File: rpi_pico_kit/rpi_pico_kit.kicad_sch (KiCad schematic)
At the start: 2 parts, among them U1 Pico, U2 RP2040

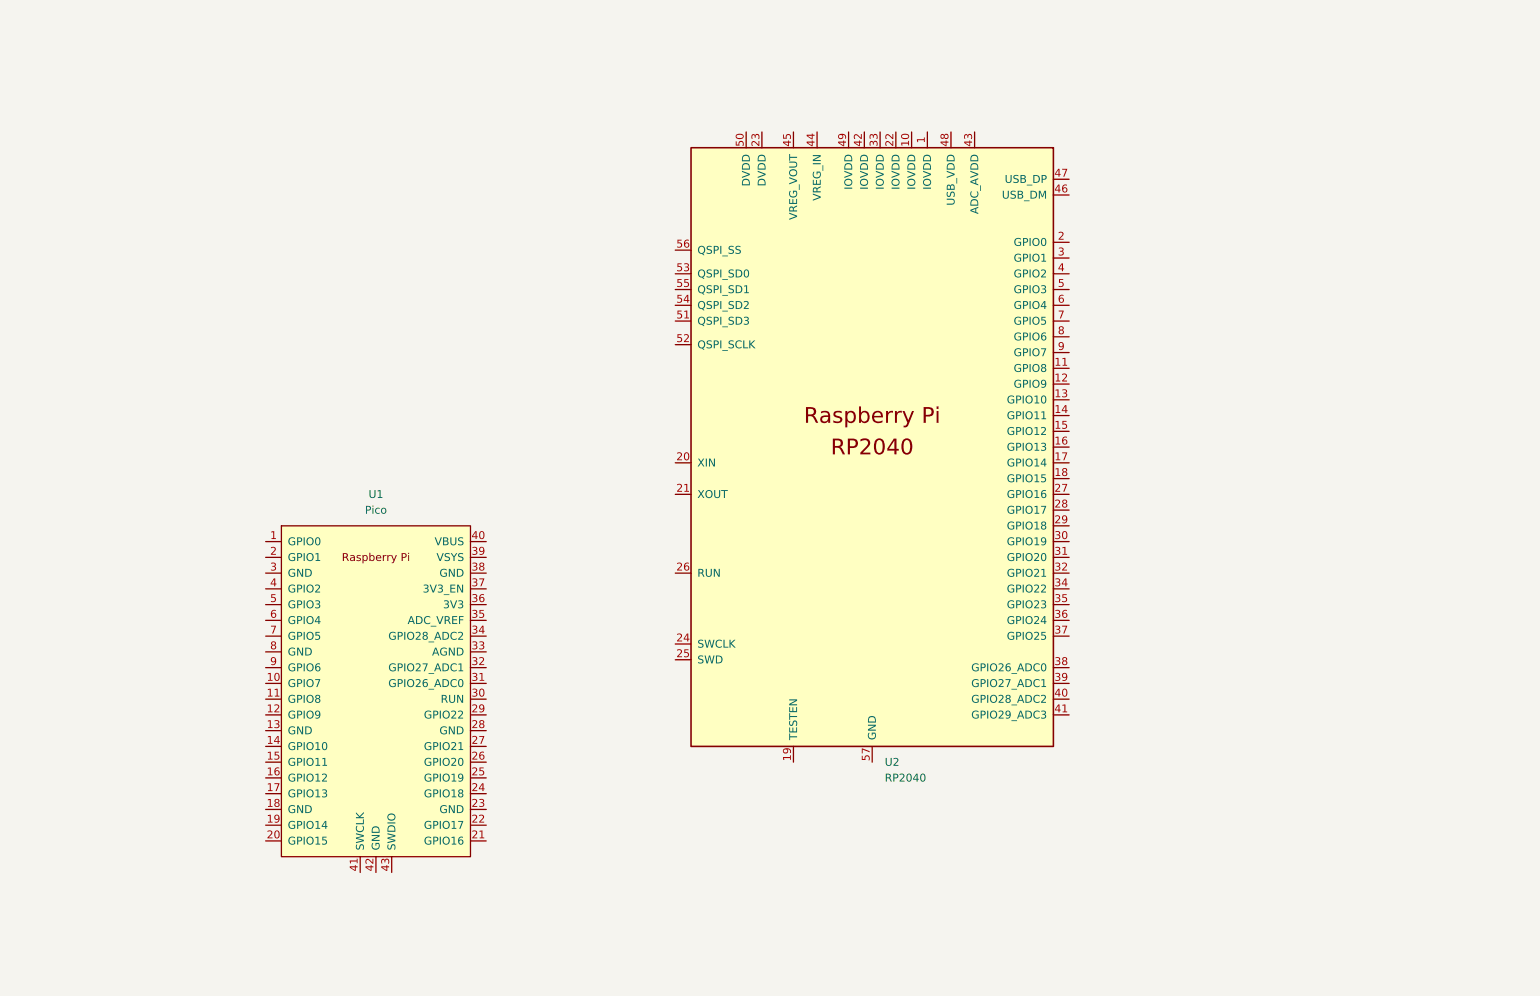
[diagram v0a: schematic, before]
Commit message: added second rpi pico as debugger
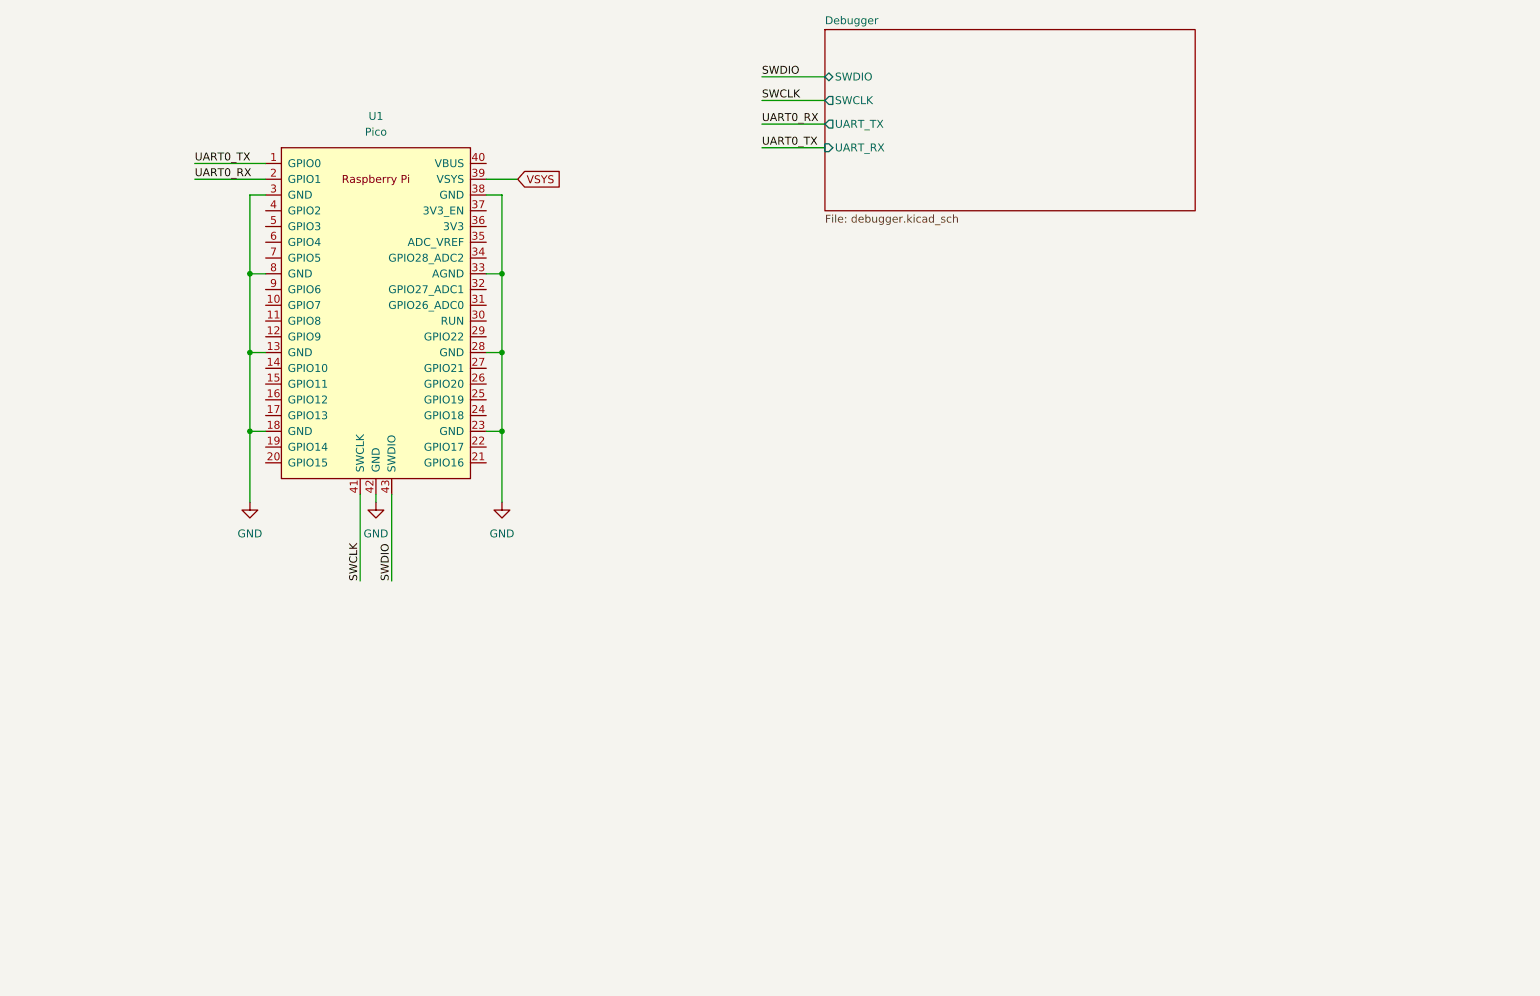
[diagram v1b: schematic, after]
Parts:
- removed U2: RP2040, RP2040_minimal:RP2040-QFN-56, symbol MCU_RaspberryPi_RP2040:RP2040
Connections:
- net UART0_TX: now reaches U1.1 (GPIO0)
- net GND: now reaches U1.13 (GND)
- net GND: now also U1.18 (GND), U1.23 (GND), U1.28 (GND), U1.3 (GND), U1.33 (AGND), U1.38 (GND), U1.42 (GND), U1.8 (GND)
- net UART0_RX: now reaches U1.2 (GPIO1)
- net VSYS: now reaches U1.39 (VSYS)
- net SWCLK: now reaches U1.41 (SWCLK)
- net SWDIO: now reaches U1.43 (SWDIO)
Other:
- added sheet Debugger (debugger.kicad_sch)
- moved on the sheet: U1

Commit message: added another components to schematic
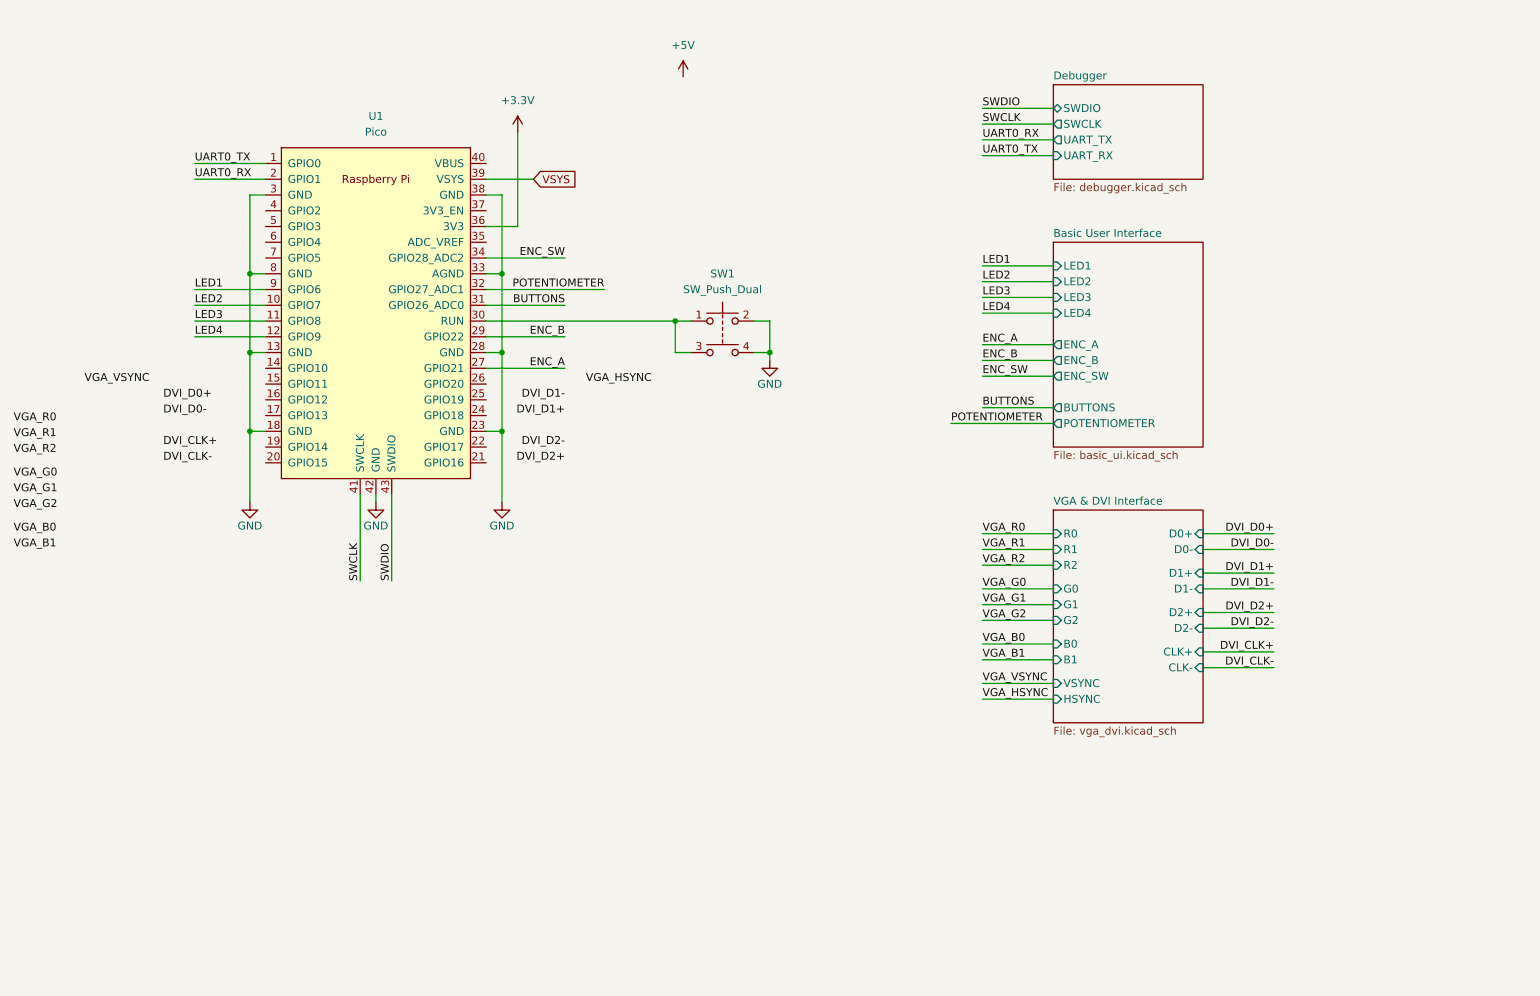
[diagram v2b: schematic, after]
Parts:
- added SW1: SW_Push_Dual, symbol Switch:SW_Push_Dual
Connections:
- net GND: now also SW1.2, SW1.4
- net LED2: now reaches U1.10 (GPIO7)
- net LED3: now reaches U1.11 (GPIO8)
- net LED4: now reaches U1.12 (GPIO9)
- net ENC_A: now reaches U1.27 (GPIO21)
- net ENC_B: now reaches U1.29 (GPIO22)
- net at U1.30 (RUN): now also SW1.1, SW1.3
- net BUTTONS: now reaches U1.31 (GPIO26_ADC0)
- net POTENTIOMETER: now reaches U1.32 (GPIO27_ADC1)
- net ENC_SW: now reaches U1.34 (GPIO28_ADC2)
- net +3V3: now reaches U1.36 (3V3)
- net LED1: now reaches U1.9 (GPIO6)
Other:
- added sheet Basic User Interface (basic_ui.kicad_sch)
- added sheet VGA & DVI Interface (vga_dvi.kicad_sch)
